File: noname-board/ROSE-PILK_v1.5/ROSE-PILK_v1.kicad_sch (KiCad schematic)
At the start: 4 parts, among them J2 Conn_01x03, SW1 SW_Push, SW2 SW_Push

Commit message: Big changes
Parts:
- removed J2 (x2): Conn_01x03, Connector_PinHeader_2.00mm:PinHeader_1x03_P2.00mm_Vertical, symbol Connector_Generic:Conn_01x03
- removed SW1, SW2: SW_Push, PS1024ALRED:SW_PS1024ALRED, symbol Switch:SW_Push
- added D18: WP154A4SUREQBFZGC, WP154A4SUREQBFZGC:LED_WP154A4SUREQBFZGC, symbol WP154A4SUREQBFZGC:WP154A4SUREQBFZGC
- added R1, R2, R3: R, Resistor_THT:R_Axial_DIN0207_L6.3mm_D2.5mm_P10.16mm_Horizontal, symbol Device:R
- added U1: Pico, MCU_RaspberryPi_and_Boards:RPi_Pico_SMD_TH, symbol MCU_RaspberryPi_and_Boards:Pico
- added U6: Pico, MarblePIco:MarblePico, symbol MCU_RaspberryPi_and_Boards:Pico
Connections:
- net GND: now also D18.2, U1.13 (GND), U1.18 (GND), U1.23 (GND), U1.28 (GND), U1.3 (GND), U1.33 (AGND), U1.38 (GND), U1.8 (GND), U6.13 (GND), U6.18 (GND), U6.23 (GND), U6.28 (GND), U6.3 (GND), U6.33 (AGND), U6.38 (GND), U6.8 (GND)
- new net: D18.3, R2.2
- new net: D18.1, R3.2
- new net: D18.4, R1.2
- no-connect marks 0 -> 6
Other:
- removed sheet BOOTSEL
- removed sheet BOOTSEL1
- removed sheet Flash Memory
- removed sheet Flash Memory1
- removed sheet LCD_Connector
- removed sheet LED Arrray
- removed sheet RP2040
- removed sheet RP2041
- removed sheet SD Card Reader
- removed sheet USBC
- sheet power ports: added none; removed 3V3, USB_IN
- note removed: "RP2040-A"
- note removed: "RP2040-A Comm Pins"
- note removed: "RP2040-B"
- note removed: "RP2040-B Comm Pins"
- note removed: "SD Card Reader"

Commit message: Completed Picos?
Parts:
- renumbered D18 to D16
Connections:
- net A10: now also U1.14 (GPIO10)
- net A11: now also U1.15 (GPIO11)
- net A12: now also U1.16 (GPIO12), U1.29 (GPIO22)
- net A26: now also U1.31 (GPIO26_ADC0)
- net A27: now also U1.32 (GPIO27_ADC1)
- net A28: now also U1.34 (GPIO28_ADC2)
- net A6: now also U1.9 (GPIO6)
- net A7: now also U1.10 (GPIO7)
- net A8: now also U1.11 (GPIO8)
- net A9: now also U1.12 (GPIO9)
- net B10: now also U6.14 (GPIO10)
- net B11: now also U6.15 (GPIO11)
- net B12: now also U6.16 (GPIO12)
- net B13: now also U6.17 (GPIO13)
- net B14: now also U6.19 (GPIO14)
- net B15: now also U6.20 (GPIO15)
- net B16: now also U6.21 (GPIO16)
- net B17: now also U6.22 (GPIO17)
- net B18: now also U6.24 (GPIO18)
- net B19: now also U6.25 (GPIO19)
- net B20: now also U6.26 (GPIO20)
- net B21: now also U6.27 (GPIO21)
- net B22: now also U6.29 (GPIO22)
- net B26: now also U6.31 (GPIO26_ADC0)
- net B27: now also U6.32 (GPIO27_ADC1)
- net B28: now also U6.34 (GPIO28_ADC2)
- net B6: now also U6.9 (GPIO6)
- net B7: now also U6.10 (GPIO7)
- net B8: now also U6.11 (GPIO8)
- net B9: now also U6.12 (GPIO9)
- net CAN1_RX: now also U1.19 (GPIO14)
- net CAN1_TX: now also U1.20 (GPIO15)
- net CAN2_RX: now also U1.21 (GPIO16)
- net CAN2_TX: now also U1.22 (GPIO17)
- net DR16-RX: now also U1.17 (GPIO13)
- net GPIO0-A: now also U1.1 (GPIO0)
- net GPIO0-B: now also U6.1 (GPIO0)
- net GPIO1-A: now also U1.2 (GPIO1)
- net GPIO1-B: now also U6.2 (GPIO1)
- net GPIO2-A: now also U1.4 (GPIO2)
- net GPIO2-B: now also U6.4 (GPIO2)
- net GPIO3-A: now also U1.5 (GPIO3)
- net GPIO3-B: now also U6.5 (GPIO3)
- net GPIO4-A: now also U1.6 (GPIO4)
- net GPIO4-B: now also U6.6 (GPIO4)
- net GPIO5-A: now also U1.7 (GPIO5)
- net GPIO5-B: now also U6.7 (GPIO5)
- net GPIO18-A: now reaches U1.24 (GPIO18)
- net GPIO19-A: now reaches U1.25 (GPIO19)
- net GPIO20-A: now reaches U1.26 (GPIO20)
- net GPIO21-A: now reaches U1.27 (GPIO21)
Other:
- note added: "Pins for Ben to deal with"
- note added: "Pins freed by lack of LED Array"
- note added: "RP2040-A Comm Pins"
- note added: "RP2040-B Comm Pins"
- moved on the sheet: U1, U6

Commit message: changez
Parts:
- added R46, R47: 0, Resistor_THT:R_Axial_DIN0207_L6.3mm_D2.5mm_P10.16mm_Horizontal, symbol Device:R
- U1: footprint MCU_RaspberryPi_and_Boards:RPi_Pico_SMD_TH -> appended_pico:Updated_Pico
- U6: footprint MarblePIco:MarblePico -> appended_pico:Updated_Pico
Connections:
- net 5V: now also U1.39 (VSYS), U6.39 (VSYS)
- net A10: no longer U1.14 (GPIO10)
- net A11: no longer U1.15 (GPIO11)
- net A12: no longer U1.29 (GPIO22)
- net A26: no longer U1.31 (GPIO26_ADC0)
- net A27: no longer U1.32 (GPIO27_ADC1)
- net A28: no longer U1.34 (GPIO28_ADC2)
- net A6: no longer U1.9 (GPIO6)
- net A7: no longer U1.10 (GPIO7)
- net A8: no longer U1.11 (GPIO8)
- net A9: no longer U1.12 (GPIO9)
- net B10: no longer U6.14 (GPIO10)
- net B11: no longer U6.15 (GPIO11)
- net B12: no longer U6.16 (GPIO12)
- net B13: no longer U6.17 (GPIO13)
- net B14: no longer U6.19 (GPIO14)
- net B15: no longer U6.20 (GPIO15)
- net B16: no longer U6.21 (GPIO16)
- net B17: no longer U6.22 (GPIO17)
- net B18: no longer U6.24 (GPIO18)
- net B19: no longer U6.25 (GPIO19)
- net B20: no longer U6.26 (GPIO20)
- net B21: no longer U6.27 (GPIO21)
- net B22: no longer U6.29 (GPIO22)
- net B26: no longer U6.31 (GPIO26_ADC0)
- net B27: no longer U6.32 (GPIO27_ADC1)
- net B28: no longer U6.34 (GPIO28_ADC2)
- net B6: no longer U6.9 (GPIO6)
- net B7: no longer U6.10 (GPIO7)
- net B8: no longer U6.11 (GPIO8)
- net B9: no longer U6.12 (GPIO9)
- net CAN1_RX: no longer U1.19 (GPIO14)
- net CAN1_TX: no longer U1.20 (GPIO15)
- net CAN2_RX: no longer U1.21 (GPIO16)
- net CAN2_TX: no longer U1.22 (GPIO17)
- net DR16-RX: no longer U1.17 (GPIO13)
- net GPIO0-A: now also R46.1; no longer U1.1 (GPIO0)
- net GPIO0-B: now also R47.2; no longer U6.1 (GPIO0)
- net GPIO1-A: now also R47.1; no longer U1.2 (GPIO1)
- net GPIO1-B: now also R46.2; no longer U6.2 (GPIO1)
- net GPIO18-A: no longer names the net of U1.24 (GPIO18)
- net GPIO19-A: no longer names the net of U1.25 (GPIO19)
- net GPIO2-A: no longer names the net of U1.4 (GPIO2)
- net GPIO2-B: no longer names the net of U6.4 (GPIO2)
- net GPIO20-A renamed A20
- net GPIO21-A: no longer names the net of U1.27 (GPIO21)
- net GPIO3-A: no longer names the net of U1.5 (GPIO3)
- net GPIO3-B: no longer names the net of U6.5 (GPIO3)
- net GPIO4-A: no longer names the net of U1.6 (GPIO4)
- net GPIO4-B: no longer names the net of U6.6 (GPIO4)
- net GPIO5-A: no longer names the net of U1.7 (GPIO5)
- net GPIO5-B: no longer names the net of U6.7 (GPIO5)
- new net A13: U1.17 (GPIO13)
- no-connect marks 6 -> 22
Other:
- removed sheet RP2040-Connect
- added sheet JETSON_UART (JETSON_UART.kicad_sch)
- sheet Power_Connectors ports: added none; removed 3V3
- note added: "4 pins reserved for sd card"
- note added: "Marble Spec Do not use"
- note removed: "Pins for Ben to deal with"
- note removed: "Pins freed by lack of LED Array"
- note removed: "RP2040-A Comm Pins"
- note removed: "RP2040-B Comm Pins"

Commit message: commit
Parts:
- renumbered R46 to R4, R47 to R5
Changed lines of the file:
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@@
   (symbol (lib_id "Device:R") (at 162.56 83.82 90) (unit 1)
     (in_bom yes) (on_board yes) (dnp no)
-    (property "Reference" "R46" (at 162.56 78.74 90)
+    (property "Reference" "R4" (at 162.56 78.74 90)
       (effects (font (size 1.27 1.27)))
     )
@@
   (symbol (lib_id "Device:R") (at 162.56 93.98 90) (unit 1)
     (in_bom yes) (on_board yes) (dnp no)
-    (property "Reference" "R47" (at 162.56 88.9 90)
+    (property "Reference" "R5" (at 162.56 88.9 90)
       (effects (font (size 1.27 1.27)))
     )

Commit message: TRACING PLACING AND OTHER SHIT I CAN'T BE BOTHERED DESCRIBING
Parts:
- added J10, J11: Conn_02x02_Counter_Clockwise, Connector_PinSocket_2.00mm:PinSocket_2x02_P2.00mm_Vertical, symbol Connector_Generic:Conn_02x02_Counter_Clockwise
- added J9: Conn_01x03, Connector_PinSocket_2.00mm:PinSocket_1x03_P2.00mm_Vertical, symbol Connector_Generic:Conn_01x03
- added SW1, SW2: SW_Push, PS1024ALRED:SW_PS1024ALRED, symbol Switch:SW_Push
- R1: value R -> 250
- R2: value R -> 220
- R3: value R -> 333
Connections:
- net 3V3: now also U1.36 (3V3), U6.36 (3V3)
- net 5V: now also J11.1 (Pin_1), J11.2 (Pin_2), J11.3 (Pin_3), J11.4 (Pin_4), J9.2 (Pin_2)
- net A26: now also U1.31 (GPIO26_ADC0)
- net A27: now also U1.32 (GPIO27_ADC1)
- net A28: now also U1.34 (GPIO28_ADC2)
- net B12: now also U6.16 (GPIO12)
- net B13: now also U6.17 (GPIO13)
- net B14: now also U6.19 (GPIO14)
- net B26: now also U6.31 (GPIO26_ADC0)
- net B27: now also U6.32 (GPIO27_ADC1)
- net B28: now also U6.34 (GPIO28_ADC2)
- net B8: now also U6.11 (GPIO8)
- net CAN1_RX: now also U1.9 (GPIO6), U6.9 (GPIO6)
- net CAN1_TX: now also U1.10 (GPIO7), U6.10 (GPIO7)
- net CAN2_RX: now also U1.14 (GPIO10), U6.14 (GPIO10)
- net CAN2_TX: now also U1.15 (GPIO11), U6.15 (GPIO11)
- net GND: now also J10.1 (Pin_1), J10.2 (Pin_2), J10.3 (Pin_3), J10.4 (Pin_4), J9.3 (Pin_3), SW1.2, SW2.2
- net GPIO0-A: now also U6.1 (GPIO0)
- net GPIO0-B: now also U1.1 (GPIO0)
- net GPIO1-A: now also U6.2 (GPIO1)
- net GPIO1-B: now also U1.2 (GPIO1)
- net LEDB: now reaches R2.1
- net LEDB: now also U6.29 (GPIO22)
- net DR16-TX: now reaches U6.12 (GPIO9)
- net LEDR: now reaches U6.26 (GPIO20)
- net LEDR: now also R3.1
- net LEDG: now reaches U6.27 (GPIO21)
- net LEDG: now also R1.1
- net at U6.30 (RUN): now also SW2.1
- net QUADA1: now reaches U6.4 (GPIO2)
- net QUADB1: now reaches U6.5 (GPIO3)
- net QUADA2: now reaches U6.6 (GPIO4)
- net QUADB2: now reaches U6.7 (GPIO5)
- net JETSON_rx: now reaches U1.11 (GPIO8)
- net JETSON_tx: now reaches U1.12 (GPIO9)
- net SERVO: now reaches U1.19 (GPIO14)
- net SERVO: now also J9.1 (Pin_1)
- net A21: now reaches U1.27 (GPIO21)
- net A22: now reaches U1.29 (GPIO22)
- net at U1.30 (RUN): now also SW1.1
- net INT: now reaches U1.4 (GPIO2)
- net ADR: now reaches U1.5 (GPIO3)
- net PS0: now reaches U1.6 (GPIO4)
- net PS1: now reaches U1.7 (GPIO5)
- net A12 renamed IMU_SDA
- net A13 renamed IMU_SCL
- net A20 renamed IMU_RST
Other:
- removed sheet Power_Connectors
- added sheet QUAD (QUAD.kicad_sch)
- sheet DR16 ports: added USART TX; removed USART RX
- sheet GPIO_Connect ports: added A_GPIO21, A_GPIO22; removed A_GPIO10, A_GPIO11, A_GPIO12, A_GPIO29, A_GPIO6, A_GPIO7, A_GPIO8, A_GPIO9, B_GPIO10, B_GPIO11, B_GPIO15, B_GPIO16, B_GPIO17, B_GPIO18, B_GPIO19, B_GPIO20, B_GPIO21, B_GPIO22, B_GPIO23, B_GPIO24, B_GPIO25, B_GPIO29, B_GPIO6, B_GPIO7, B_GPIO9
- note added: "IMU_SCL"
- note added: "IMU_SDA"
- note added: "Servo PWM"
- moved on the sheet: D16, R1, R2, R3, R4, R5, U1, U6

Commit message: Post Mark Crosby
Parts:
- renumbered J10 to J12, J11 to J13
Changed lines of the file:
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@@
   (symbol (lib_id "Connector_Generic:Conn_02x02_Counter_Clockwise") (at 90.17 134.62 0) (unit 1)
     (in_bom yes) (on_board yes) (dnp no) (fields_autoplaced)
-    (property "Reference" "J11" (at 91.44 128.27 0)
+    (property "Reference" "J13" (at 91.44 128.27 0)
       (effects (font (size 1.27 1.27)))
     )
@@
   (symbol (lib_id "Connector_Generic:Conn_02x02_Counter_Clockwise") (at 90.17 148.59 0) (unit 1)
     (in_bom yes) (on_board yes) (dnp no) (fields_autoplaced)
-    (property "Reference" "J10" (at 91.44 142.24 0)
+    (property "Reference" "J12" (at 91.44 142.24 0)
       (effects (font (size 1.27 1.27)))
     )

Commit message: Tracing part 2
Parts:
- added 5VCAP1, IMUC13, PICOU1, PICOU6, SERVO1: .1uF, Capacitor_THT:C_Disc_D7.0mm_W2.5mm_P5.00mm, symbol Device:C
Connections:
- net 3V3: now also IMUC13.1
- net 5V: now also 5VCAP1.1, 5VCAP1.2, PICOU1.1, PICOU6.1, SERVO1.2
- net GND: now also IMUC13.2, PICOU1.2, PICOU6.2, SERVO1.1

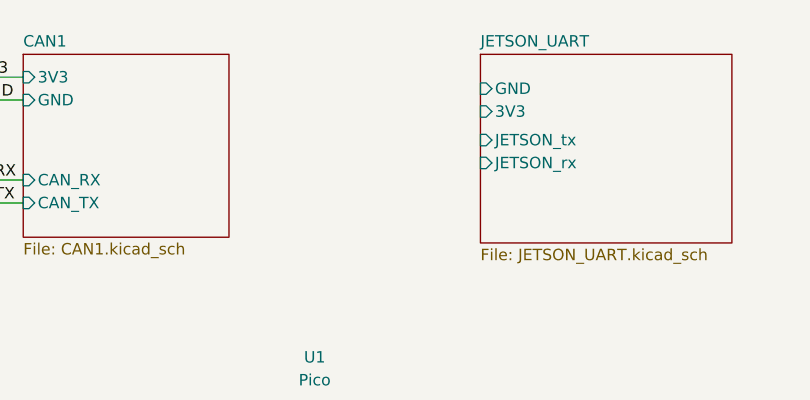
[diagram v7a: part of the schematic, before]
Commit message: redid some of the traces
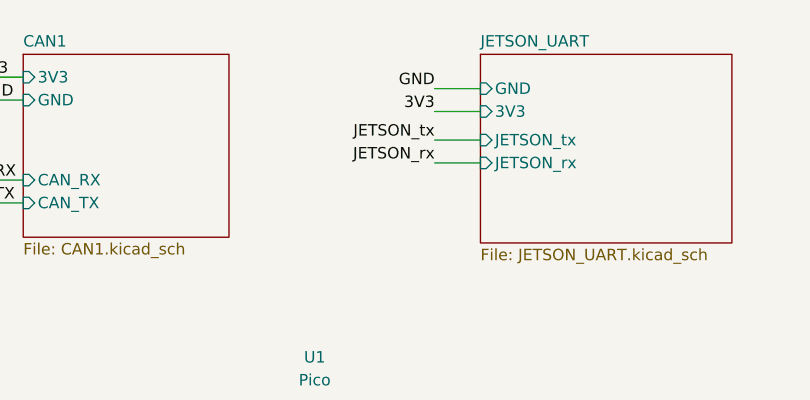
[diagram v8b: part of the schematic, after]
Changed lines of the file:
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@@
+    (stroke (width 0) (type default))
+  )
+  (wire (pts (xy 109.855 29.21) (xy 114.935 29.21))
     (stroke (width 0) (type default))
   )
@@
     (stroke (width 0) (type default))
   )
+  (wire (pts (xy 109.855 23.495) (xy 114.935 23.495))
+    (stroke (width 0) (type default))
+  )
   (wire (pts (xy 114.3 106.68) (xy 127 106.68))
     (stroke (width 0) (type default))
@@
     (stroke (width 0) (type default))
   )
+  (wire (pts (xy 109.855 20.955) (xy 114.935 20.955))
+    (stroke (width 0) (type default))
+  )
   (wire (pts (xy 204.47 102.87) (xy 208.28 102.87))
     (stroke (width 0) (type default))
@@
     (stroke (width 0) (type default))
   )
+  (wire (pts (xy 109.855 26.67) (xy 114.935 26.67))
+    (stroke (width 0) (type default))
+  )
   (wire (pts (xy 243.84 67.31) (xy 259.08 67.31))
     (stroke (width 0) (type default))
@@
     (effects (font (size 1.27 1.27)) (justify left bottom))
   )
+  (label "JETSON_tx" (at 109.855 26.67 180) (fields_autoplaced)
+    (effects (font (size 1.27 1.27)) (justify right bottom))
+  )
   (label "CAN1_RX" (at 55.245 31.115 0) (fields_autoplaced)
     (effects (font (size 1.27 1.27)) (justify left bottom))
@@
     (effects (font (size 1.27 1.27)) (justify left bottom))
   )
+  (label "3V3" (at 109.855 23.495 180) (fields_autoplaced)
+    (effects (font (size 1.27 1.27)) (justify right bottom))
+  )
   (label "QUADB2" (at 194.31 74.93 0) (fields_autoplaced)
     (effects (font (size 1.27 1.27)) (justify left bottom))
@@
     (effects (font (size 1.27 1.27)) (justify left bottom))
   )
+  (label "GND" (at 109.855 20.955 180) (fields_autoplaced)
+    (effects (font (size 1.27 1.27)) (justify right bottom))
+  )
   (label "GND" (at 97.79 148.59 0) (fields_autoplaced)
     (effects (font (size 1.27 1.27)) (justify left bottom))
@@
     (effects (font (size 1.27 1.27)) (justify left bottom))
   )
+  (label "JETSON_rx" (at 109.855 29.21 180) (fields_autoplaced)
+    (effects (font (size 1.27 1.27)) (justify right bottom))
+  )
   (label "5V" (at 23.495 52.07 0) (fields_autoplaced)
